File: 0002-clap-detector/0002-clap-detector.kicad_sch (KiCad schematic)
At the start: 0 parts

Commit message: Electric schematic
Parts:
- added C1, C2, C3, C4: 100n, symbol Device:C
- added C5: 100u, symbol Device:C_Polarized
- added D1: GREEN, symbol Device:LED
- added D2: RED, symbol Device:LED
- added D3: 1N4148, symbol Device:D
- added J1: 9V, symbol Device:Battery_Cell
- added J2: OUT, symbol Connector:Screw_Terminal_01x02
- added K1: HF49FD 012-1H11, symbol Relay:Relay_SPST-NO
- added MK1: ~, symbol Device:Microphone
- added Q1, Q2, Q4: BC847B, symbol Simulation_SPICE:NPN
- added Q3: BCV26, symbol Simulation_SPICE:PNP
- added R1: 10k, symbol Device:R
- added R10: 4,7k, symbol Device:R
- added R2, R3, R4, R5, R8: 100k, symbol Device:R
- added R6: 47k, symbol Device:R
- added R7: 10M, symbol Device:R
- added R9: 1k, symbol Device:R
- added TP1: 6..11V, symbol Connector:TestPoint
- added TP2: 3,85V, symbol Connector:TestPoint
- added TP3: 11,4V, symbol Connector:TestPoint
- added TP4: 3,3V, symbol Connector:TestPoint
- added TP5: ~, symbol Connector:TestPoint
- added TP6: 2,6V, symbol Connector:TestPoint
- added TP7: 0V, symbol Connector:TestPoint
- added TP8, TP9: 10,5V, symbol Connector:TestPoint
- added U1: 4017, symbol 4xxx:4017
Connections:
- new net: C2.1, Q1.3 (E), R4.1, TP4.1
- new net: Q2.3 (E), R4.2, R8.1, TP6.1, U1.14 (CLK)
- new net: C3.2, R5.1, TP7.1, U1.15 (Reset)
- new net: R5.2, U1.4 (Q2)
- new net: D3.2 (A), K1.A2, Q4.1 (C)
- new net: Q4.2 (B), R10.2
- new net: D1.2 (A), TP8.1, U1.2 (Q1)
- new net: D2.2 (A), R10.1, TP9.1, U1.3 (Q0)
- new net: C4.1, Q2.2 (B), Q3.1 (C), R7.1, TP5.1
- new net: D1.1 (K), D2.1 (K), R9.1
- new net: J2.2 (Pin_2), K1.13
- new net: J2.1 (Pin_1), K1.14
- new net: Q1.1 (C), Q3.2 (B), R3.2, TP3.1
- new net: C1.1, Q1.2 (B), R2.2, R6.1, TP2.1
- new net: C1.2, MK1.2 (+), R1.2, TP1.1
- new net GNDD: C2.2, C4.2, C5.2, J1.2 (-), MK1.1 (-), Q4.3 (E), R6.2, R7.2, R8.2, R9.2, U1.13 (CKEN), U1.8 (VSS)
- new net VDD: C3.1, C5.1, D3.1 (K), J1.1 (+), K1.A1, Q2.1 (C), Q3.3 (E), R1.1, R2.1, R3.1, U1.16 (VDD)
- no-connect marks 0 -> 8
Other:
- company: (none) -> ${GH_REPO}
- title: (none) -> Clap detector

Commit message: Schematics
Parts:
- MK1: value ~ -> BCM-9765P
- TP5: value ~ -> ?
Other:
- moved on the sheet: C3, R4, R5, TP1, TP2, TP3, TP4, TP5, TP6, TP7, TP8, TP9

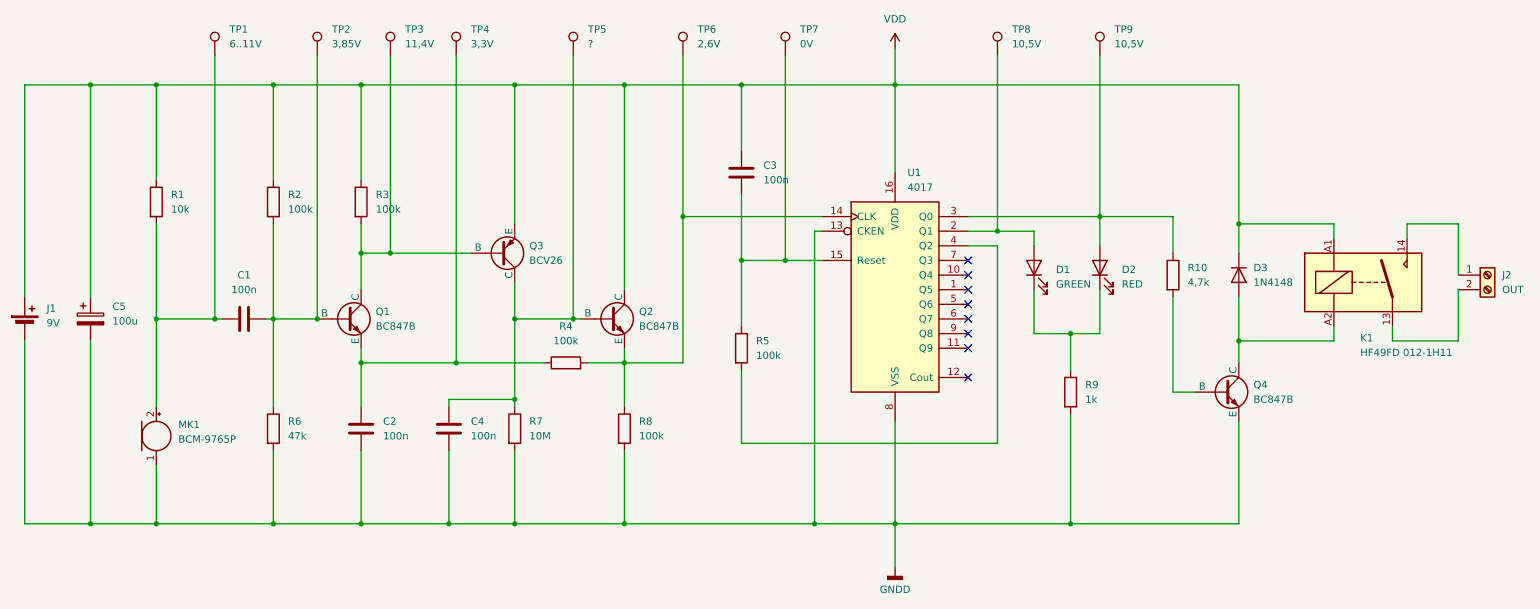
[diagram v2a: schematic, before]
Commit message: Assign footprints to components (#3)
Co-authored-by: Marcin Ciapa <aaryndo@gmail.com>
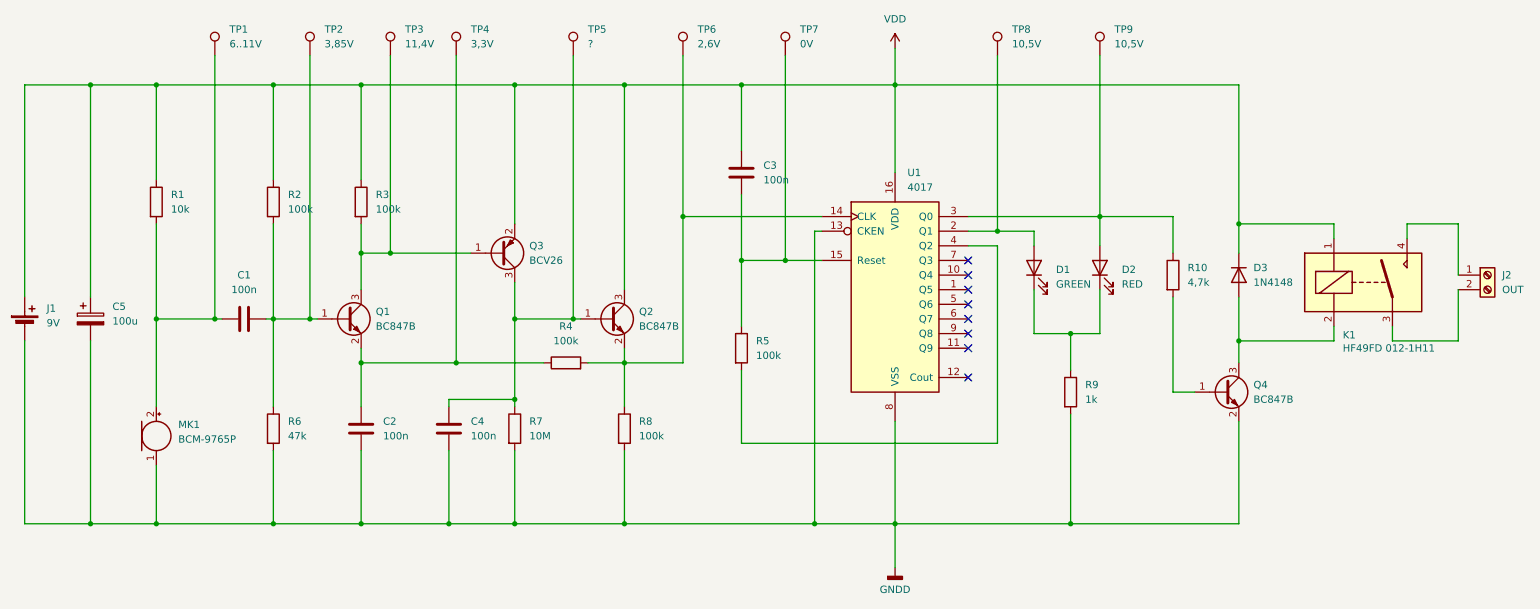
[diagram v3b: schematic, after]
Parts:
- removed K1: HF49FD 012-1H11, symbol Relay:Relay_SPST-NO
- removed Q1, Q2, Q4: BC847B, symbol Simulation_SPICE:NPN
- removed Q3: BCV26, symbol Simulation_SPICE:PNP
- added K1: HF49FD 012-1H11, Relay_THT:Relay_SPST_TE_PCN-1xxD3MHZ, symbol 0002-clap-detector.kicad:HF49FD
- added Q1, Q2, Q4: BC847B, Package_TO_SOT_SMD:SOT-23, symbol Transistor_BJT:BC847
- added Q3: BCV26, Package_TO_SOT_SMD:SOT-23, symbol Transistor_BJT:BC857
- C1, C2, C3, C4: footprint (none) -> Capacitor_SMD:C_0805_2012Metric_Pad1.18x1.45mm_HandSolder
- C5: footprint (none) -> Capacitor_Tantalum_SMD:CP_EIA-6032-28_Kemet-C_HandSolder
- D1, D2: footprint (none) -> LED_SMD:LED_0805_2012Metric_Pad1.15x1.40mm_HandSolder
- D3: footprint (none) -> Diode_SMD:D_SOD-323_HandSoldering
- J1: footprint (none) -> Connector_JST:JST_SH_BM02B-SRSS-TB_1x02-1MP_P1.00mm_Vertical
- J2: footprint (none) -> TerminalBlock_MetzConnect:TerminalBlock_MetzConnect_Type059_RT06302HBWC_1x02_P3.50mm_Horizontal
- MK1: footprint (none) -> LED_THT:LED_D10.0mm
- R1, R10, R2, R3, R4, R5, R6, R7, R8, R9: footprint (none) -> Resistor_SMD:R_0805_2012Metric_Pad1.20x1.40mm_HandSolder
- TP1, TP2, TP3, TP4, TP5, TP6, TP7, TP8, TP9: footprint (none) -> TestPoint:TestPoint_Pad_D1.5mm
- U1: footprint (none) -> Package_SO:SOP-16_4.4x10.4mm_P1.27mm
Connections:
- net GNDD: now also Q4.2 (E)
- net VDD: now also K1.1, Q2.3 (C), Q3.2 (E)
- net at C2.1, R4.1, TP4.1: now also Q1.2 (E)
- net at R4.2, R8.1, TP6.1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: now also Q2.2 (E)
- net at D3.2 (A): now also K1.2, Q4.3 (C)
- net at R10.2: now also Q4.1 (B)
- net at C4.1, R7.1, TP5.1: now also Q2.1 (B), Q3.3 (C)
- net at J2.2 (Pin_2): now also K1.3
- net at J2.1 (Pin_1): now also K1.4
- net at R3.2, TP3.1: now also Q1.3 (C), Q3.1 (B)
- net at C1.1, R2.2, R6.1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: now also Q1.1 (B)
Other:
- moved on the sheet: TP2
